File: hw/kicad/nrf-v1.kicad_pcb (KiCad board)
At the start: 2 copper layers, 25 parts, among them U1 TPS62732, U2 nRF51822, U3 SST25WF040B, U4 BMA280, U5 SI7053

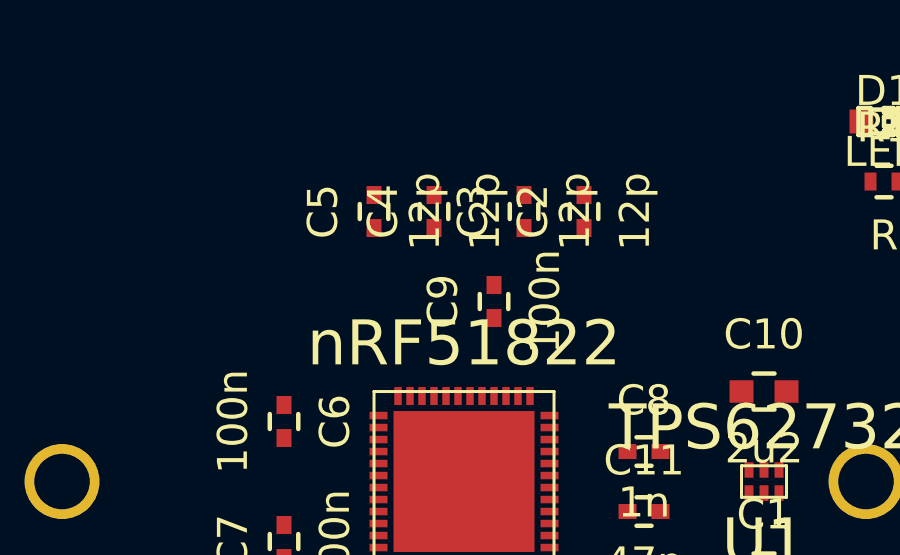
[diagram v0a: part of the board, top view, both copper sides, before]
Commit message: Add crystals
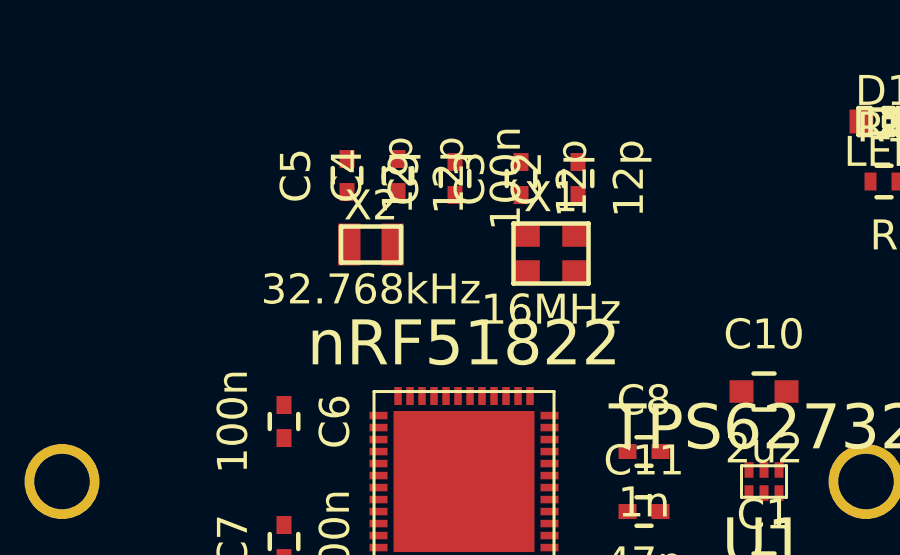
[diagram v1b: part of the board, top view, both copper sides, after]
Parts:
- added X1: 16MHz, project:Abracon-ABM10, F.Cu at (102.9, 92.4)
- added X2: 32.768kHz, project:Abracon-ABS06, F.Cu at (96.9, 92.1)
- moved C9 4.30 mm to (99.7, 89.9)
- moved C4 1.70 mm to (97.8, 89.8)
- moved C5 1.50 mm to (96.1, 89.8)
- moved C2 1.12 mm to (103.8, 89.9)
- moved C3 1.10 mm to (101.9, 89.9)
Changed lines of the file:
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@@
 (kicad_pcb (version 4) (host pcbnew "(2014-10-24 BZR 5221)-product")
   (general
-    (links 59)
-    (no_connects 59)
+    (links 65)
+    (no_connects 65)
     (area 0 0 0 0)
     (thickness 1.6)
@@
     (tracks 0)
     (zones 0)
-    (modules 25)
+    (modules 27)
     (nets 65)
   )
@@
     (mod_text_size 1 1)
     (mod_text_width 0.15)
-    (pad_size 4 4)
+    (pad_size 0.9 0.8)
     (pad_drill 0)
     (pad_to_mask_clearance 0)
@@
   )
   (module Capacitors_SMD:C_0402 (layer F.Cu)
-    (at 104 91 90)
+    (at 103.8 89.9 90)
     (descr "Capacitor SMD 0402, reflow soldering, AVX (see smccp.pdf)")
     (tags "capacitor 0402")
@@
   )
   (module Capacitors_SMD:C_0402 (layer F.Cu)
-    (at 102 91 90)
+    (at 101.9 89.9 90)
     (descr "Capacitor SMD 0402, reflow soldering, AVX (see smccp.pdf)")
     (tags "capacitor 0402")
@@
   )
   (module Capacitors_SMD:C_0402 (layer F.Cu)
-    (at 99 91 90)
+    (at 97.8 89.8 90)
     (descr "Capacitor SMD 0402, reflow soldering, AVX (see smccp.pdf)")
     (tags "capacitor 0402")
@@
   )
   (module Capacitors_SMD:C_0402 (layer F.Cu)
-    (at 97 91 90)
+    (at 96.1 89.8 90)
     (descr "Capacitor SMD 0402, reflow soldering, AVX (see smccp.pdf)")
     (tags "capacitor 0402")
@@
   )
   (module Capacitors_SMD:C_0402 (layer F.Cu)
-    (at 101 94 90)
+    (at 99.7 89.9 90)
     (descr "Capacitor SMD 0402, reflow soldering, AVX (see smccp.pdf)")
     (tags "capacitor 0402")
@@
       (net 2 GND))
   )
+  (module project:Abracon-ABM10 (layer F.Cu)
+    (at 102.9 92.4 180)
+    (fp_text reference X1 (at 0 1.875 180) (layer F.SilkS)
+      (effects (font (size 1 1) (thickness 0.15)))
+    )
+    (fp_text value 16MHz (at 0 -1.875 180) (layer F.SilkS)
+      (effects (font (size 1 1) (thickness 0.15)))
+    )
+    (fp_line (start -1.25 -1) (end 1.25 -1) (layer F.SilkS) (width 0.15))
+    (fp_line (start 1.25 -1) (end 1.25 1) (layer F.SilkS) (width 0.15))
+    (fp_line (start 1.25 1) (end -1.25 1) (layer F.SilkS) (width 0.15))
+    (fp_line (start -1.25 1) (end -1.25 -1) (layer F.SilkS) (width 0.15))
+    (pad 1 smd rect (at -0.825 0.625 180) (size 0.9 0.8) (layers F.Cu F.Paste F.Mask)
+      (net 3 "Net-(C2-Pad1)"))
+    (pad 2 smd rect (at 0.825 0.625 180) (size 0.9 0.8) (layers F.Cu F.Paste F.Mask)
+      (net 2 GND))
+    (pad 3 smd rect (at 0.825 -0.625 180) (size 0.9 0.8) (layers F.Cu F.Paste F.Mask)
+      (net 4 "Net-(C3-Pad1)"))
+    (pad 4 smd rect (at -0.825 -0.625 180) (size 0.9 0.8) (layers F.Cu F.Paste F.Mask)
+      (net 2 GND))
+  )
+  (module project:Abracon-ABS06 (layer F.Cu)
+    (at 96.9 92.1 180)
+    (fp_text reference X2 (at 0 1.3 180) (layer F.SilkS)
+      (effects (font (size 1 1) (thickness 0.15)))
+    )
+    (fp_text value 32.768kHz (at 0 -1.5 180) (layer F.SilkS)
+      (effects (font (size 1 1) (thickness 0.15)))
+    )
+    (fp_line (start -1 -0.6) (end 1 -0.6) (layer F.SilkS) (width 0.15))
+    (fp_line (start 1 -0.6) (end 1 0.6) (layer F.SilkS) (width 0.15))
+    (fp_line (start 1 0.6) (end -1 0.6) (layer F.SilkS) (width 0.15))
+    (fp_line (start -1 0.6) (end -1 -0.6) (layer F.SilkS) (width 0.15))
+    (pad 1 smd rect (at -0.725 0 180) (size 0.75 1.4) (layers F.Cu F.Paste F.Mask)
+      (net 5 "Net-(C4-Pad1)"))
+    (pad 2 smd rect (at 0.725 0 180) (size 0.75 1.4) (layers F.Cu F.Paste F.Mask)
+      (net 6 "Net-(C5-Pad1)"))
+  )
 )

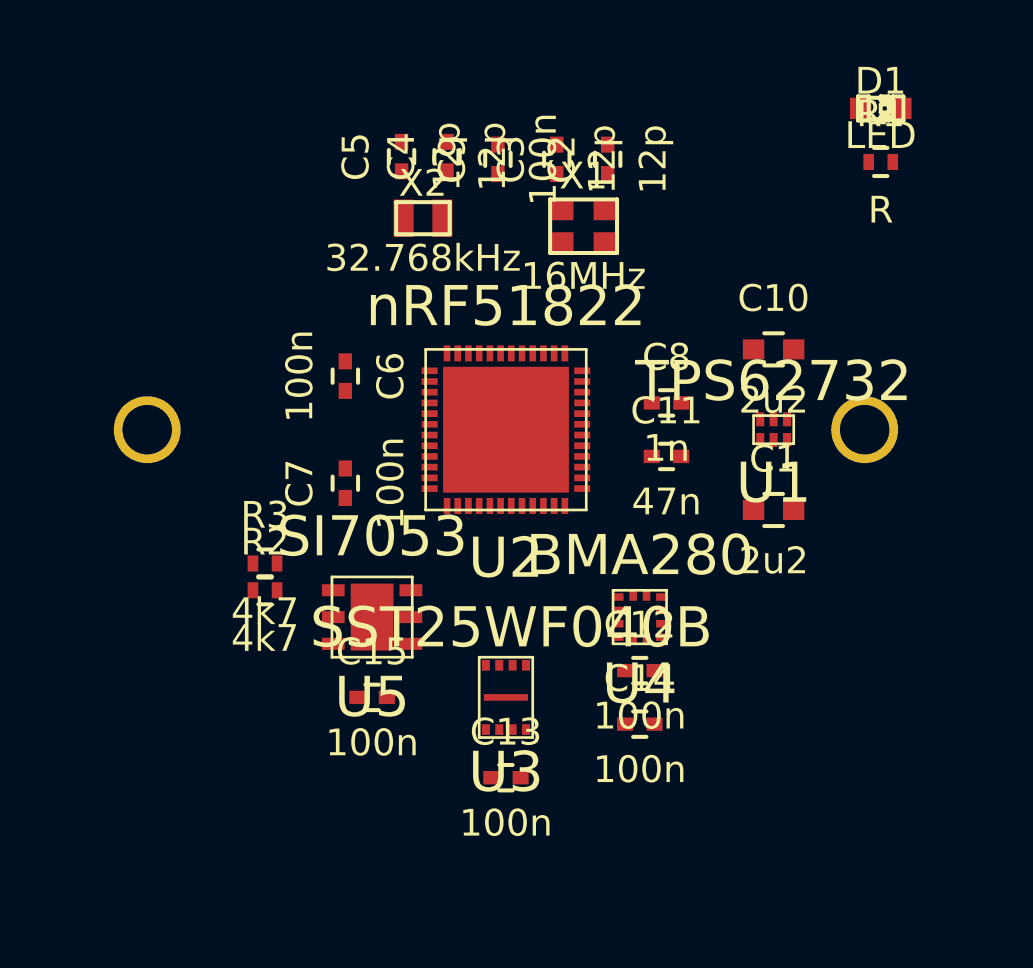
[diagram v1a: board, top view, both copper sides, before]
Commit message: Change coin cell holder
From 25mm to 20mm
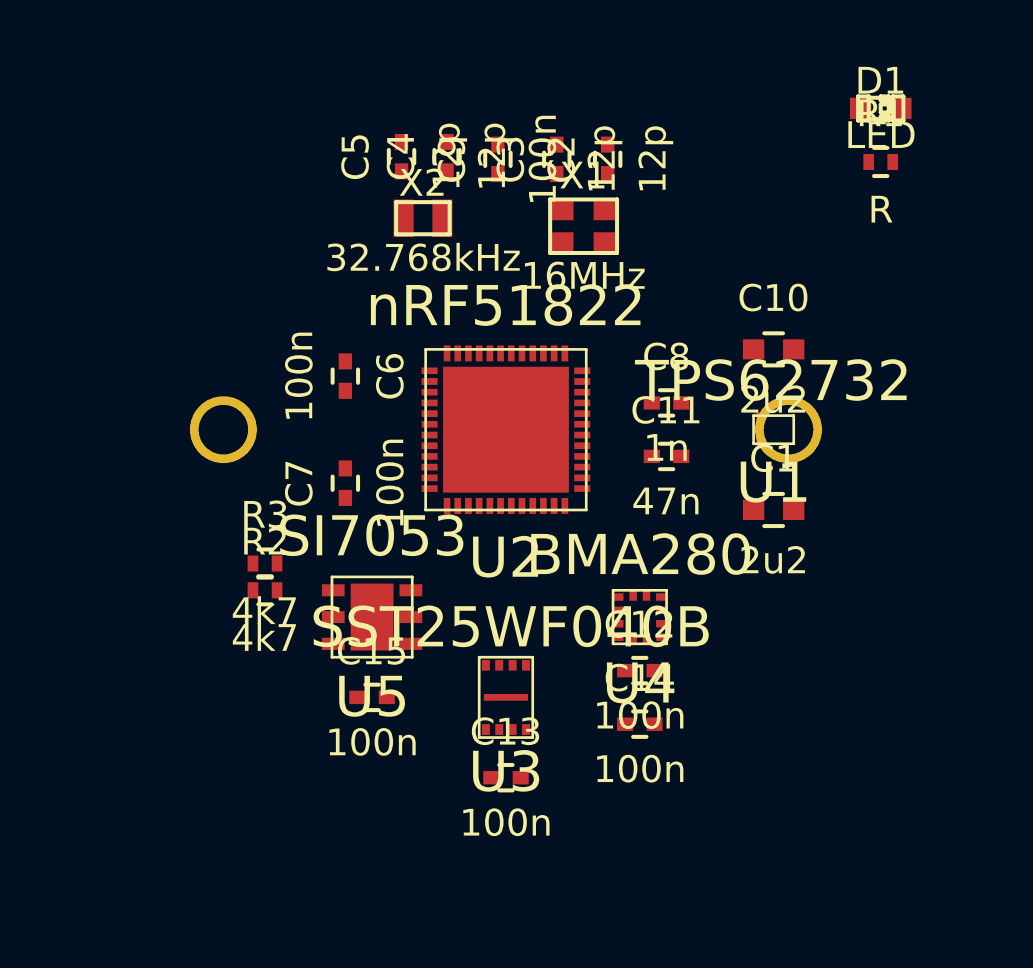
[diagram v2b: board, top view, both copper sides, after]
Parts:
- BT1: footprint project:Keystone-3007 -> project:Keystone-3003
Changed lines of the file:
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@@
   (general
     (links 65)
-    (no_connects 65)
+    (no_connects 64)
     (area 0 0 0 0)
     (thickness 1.6)
@@
     (mod_text_size 1 1)
     (mod_text_width 0.15)
-    (pad_size 0.9 0.8)
+    (pad_size 4 4)
     (pad_drill 0)
     (pad_to_mask_clearance 0)
@@
       (net 12 twi_scl))
   )
-  (module project:Keystone-3007 (layer B.Cu)
-    (at 100 100)
-    (fp_text reference BT1 (at 0.6 5.2) (layer B.SilkS)
-      (effects (font (size 1 1) (thickness 0.15)) (justify mirror))
-    )
-    (fp_text value BATTERY (at 1 6.4) (layer B.SilkS)
-      (effects (font (size 1 1) (thickness 0.15)) (justify mirror))
-    )
-    (fp_line (start 12.7 4.7) (end 11.8 4.7) (layer B.SilkS) (width 0.15))
-    (fp_line (start -12.7 4.7) (end -11.8 4.7) (layer B.SilkS) (width 0.15))
-    (fp_line (start 12.7 -4.7) (end 11.6 -4.7) (layer B.SilkS) (width 0.15))
-    (fp_line (start 11.6 -4.7) (end 3.8 -11.9) (layer B.SilkS) (width 0.15))
-    (fp_line (start -11.6 -4.7) (end -3.8 -11.9) (layer B.SilkS) (width 0.15))
-    (fp_line (start 3.8 -12.85) (end 3.8 -11.9) (layer B.SilkS) (width 0.15))
-    (fp_line (start -3.8 -12.85) (end -3.8 -11.9) (layer B.SilkS) (width 0.15))
-    (fp_line (start -12.7 -4.7) (end -11.6 -4.7) (layer B.SilkS) (width 0.15))
-    (fp_circle (center 0 0) (end 12.5 0) (layer B.SilkS) (width 0.15))
-    (fp_line (start 12.7 -4.71) (end 12.7 4.71) (layer B.SilkS) (width 0.15))
-    (fp_line (start -12.7 -4.71) (end -12.7 4.71) (layer B.SilkS) (width 0.15))
-    (fp_line (start -3.8 -12.85) (end 3.8 -12.85) (layer B.SilkS) (width 0.15))
-    (pad 1 thru_hole circle (at -13.4 0) (size 2.5 2.5) (drill 1.85) (layers *.Cu *.Mask B.SilkS)
-      (net 1 +BATT))
-    (pad 1 thru_hole circle (at 13.4 0) (size 2.5 2.5) (drill 1.85) (layers *.Cu *.Mask B.SilkS)
-      (net 1 +BATT))
-    (pad 2 smd rect (at 0 0) (size 4 4) (layers B.Cu B.Paste B.Mask)
-      (net 2 GND))
-  )
   (module project:Abracon-ABM10 (layer F.Cu)
     (at 102.9 92.4 180)
@@
       (net 6 "Net-(C5-Pad1)"))
   )
+  (module project:Keystone-3003 (layer B.Cu)
+    (at 100 100)
+    (fp_text reference BT1 (at 0.6 5.2) (layer B.SilkS)
+      (effects (font (size 1 1) (thickness 0.15)) (justify mirror))
+    )
+    (fp_text value BATTERY (at 1 6.4) (layer B.SilkS)
+      (effects (font (size 1 1) (thickness 0.15)) (justify mirror))
+    )
+    (fp_circle (center 0 0) (end 10 0) (layer B.SilkS) (width 0.15))
+    (fp_line (start -3.8 -10.58) (end 3.8 -10.58) (layer B.SilkS) (width 0.15))
+    (pad 1 thru_hole circle (at -10.555 0) (size 2.5 2.5) (drill 1.85) (layers *.Cu *.Mask B.SilkS)
+      (net 1 +BATT))
+    (pad 1 thru_hole circle (at 10.555 0) (size 2.5 2.5) (drill 1.85) (layers *.Cu *.Mask B.SilkS)
+      (net 1 +BATT))
+    (pad 2 smd rect (at 0 0) (size 4 4) (layers B.Cu B.Paste B.Mask)
+      (net 2 GND))
+  )
 )

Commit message: Component placement draft
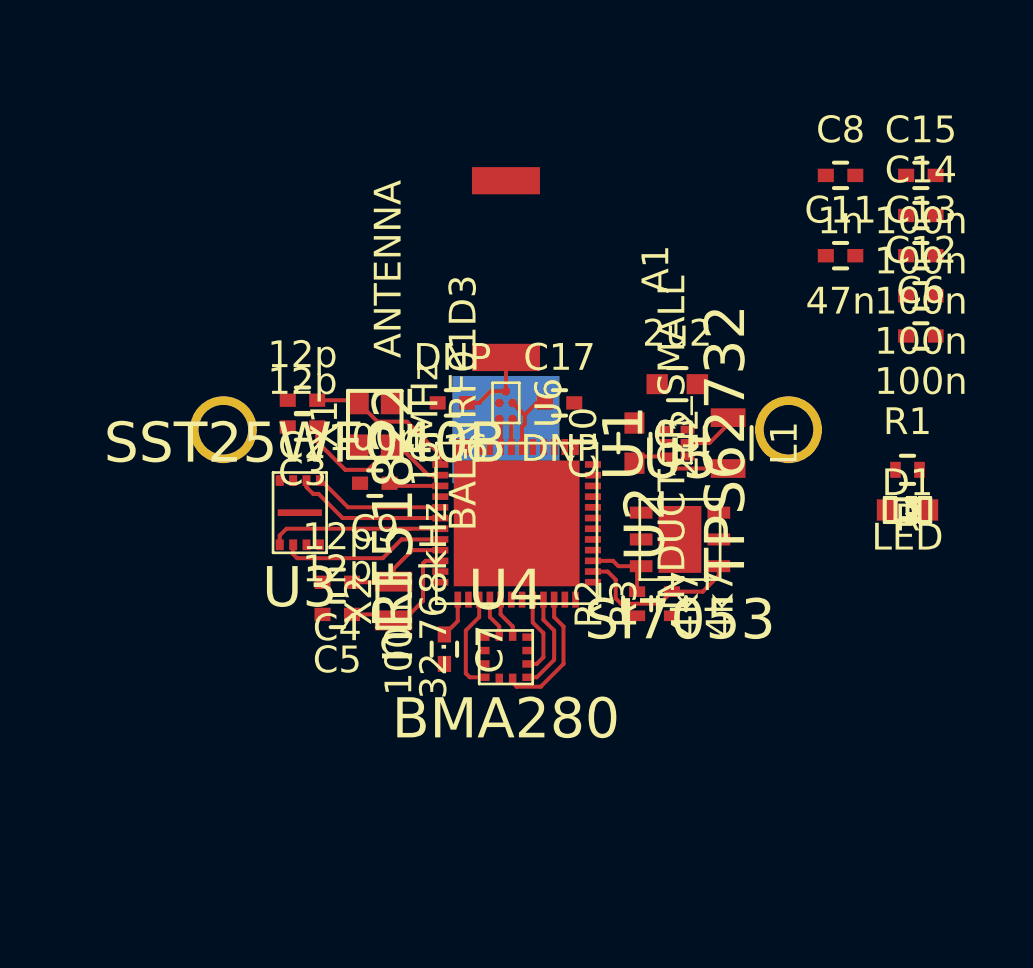
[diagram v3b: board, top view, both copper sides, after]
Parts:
- added A1: ANTENNA, project:AntennaFactor-ANT-2.4-CHP, F.Cu at (100.0, 94.0)
- added C16: DNP, Capacitors_SMD:C_0402, F.Cu at (98.0, 99.0)
- added C17: DNP, Capacitors_SMD:C_0402, F.Cu at (102.0, 99.0)
- added L1: INDUCTOR_SMALL, Resistors_SMD:R_0805, F.Cu at (108.3, 100.5)
- added U6: BAL-NRF01D3, project:ST-BGA-5_(1.50x1.00), F.Cu at (100.0, 99.0)
- moved C15 28.3 mm to (115.5, 90.5)
- moved C13 24.9 mm to (115.5, 93.5)
- moved C14 21.7 mm to (115.5, 92.0)
- moved C6 21.6 mm to (115.5, 96.5), turned to 0 degrees
- moved C12 17.5 mm to (115.5, 95.0)
- moved C5 17.3 mm to (93.7, 106.9), turned to 180 degrees
- moved C4 16.4 mm to (93.7, 105.7), turned to 180 degrees
- moved R3 15.3 mm to (106.2, 106.5), turned to 90 degrees
- moved D1 15.0 mm to (115.0, 103.0)
- moved C2 14.5 mm to (92.4, 98.9), turned to 180 degrees
- moved X2 14.3 mm to (95.8, 106.4), turned to 270 degrees
- moved R2 13.9 mm to (104.9, 106.5), turned to 90 degrees
- moved C3 13.8 mm to (92.4, 99.9), turned to 180 degrees
- moved C9 12.9 mm to (95.1, 102.0), turned to 180 degrees
- moved U5 11.9 mm to (106.5, 104.1), turned to 180 degrees
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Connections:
- C10 pad 1: Net-(C10-Pad1) -> VDD
- U2 pad 10: Net-(U2-Pad10) -> spi1_sck
- U2 pad 14: Net-(U2-Pad14) -> twi_sda
- U2 pad 15: Net-(U2-Pad15) -> twi_scl
- U2 pad 3: Net-(U2-Pad3) -> spi1_cs_n
- U2 pad 4: Net-(U2-Pad4) -> acc_int2
- U2 pad 41: Net-(U2-Pad41) -> spi0_cs_n
- U2 pad 42: Net-(U2-Pad42) -> spi0_miso
- U2 pad 43: Net-(U2-Pad43) -> spi0_mosi
- U2 pad 44: Net-(U2-Pad44) -> spi0_sck
- U2 pad 5: Net-(U2-Pad5) -> acc_int1
- U2 pad 8: Net-(U2-Pad8) -> spi1_mosi
- U2 pad 9: Net-(U2-Pad9) -> spi1_miso
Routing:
- net spi0_mosi: track 0.00 -> 6.45 mm
- net Net-(C3-Pad1): track 0.00 -> 6.39 mm
- net twi_sda: track 0.00 -> 6.39 mm
- net spi0_sck: track 0.00 -> 6.20 mm
- net Net-(C2-Pad1): track 0.00 -> 5.80 mm
- net spi0_miso: track 0.00 -> 5.73 mm
- net VDD: track 0.00 -> 5.30 mm
- net Net-(C5-Pad1): track 0.00 -> 5.13 mm
- net spi1_sck: track 0.00 -> 4.99 mm
- net spi0_cs_n: track 0.00 -> 4.91 mm
- net Net-(C4-Pad1): track 0.00 -> 4.08 mm
- net spi1_cs_n: track 0.00 -> 3.70 mm
- net spi1_miso: track 0.00 -> 3.67 mm
- net spi1_mosi: track 0.00 -> 3.00 mm
- net twi_scl: track 0.00 -> 2.89 mm
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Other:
- net class Default: clearance 0.254 -> 0.1; trace_width 0.254 -> 0.2; via_dia 0.889 -> 0.3; via_drill 0.635 -> 0.15
- rule trace_clearance: 0.254 -> 0.1
- rule trace_min: 0.254 -> 0.15
- rule via_min_drill: 0.508 -> 0.15
- rule via_min_size: 0.889 -> 0.3

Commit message: Updated coin cell holder
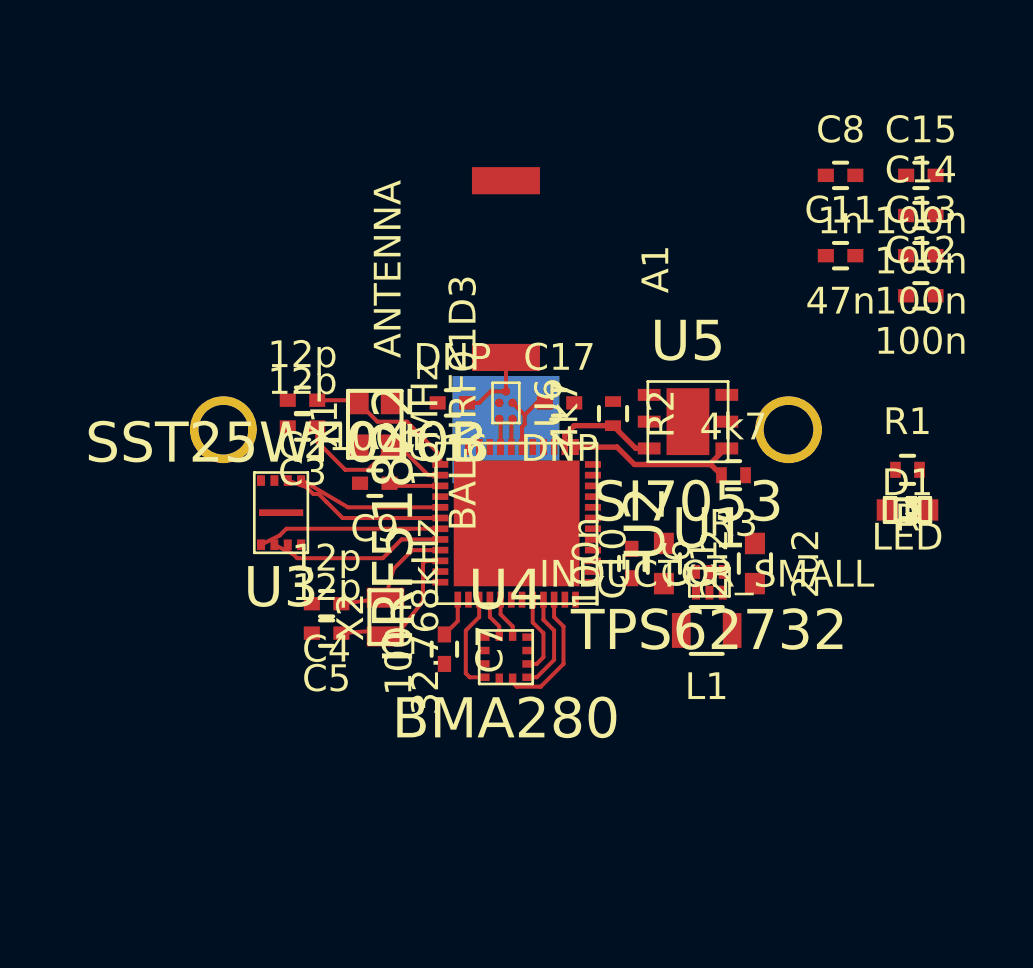
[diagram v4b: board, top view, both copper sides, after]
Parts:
- moved C6 13.7 mm to (104.7, 105.0), turned to 270 degrees
- moved C1 7.30 mm to (109.3, 105.0), turned to 90 degrees
- moved R2 7.16 mm to (104.0, 99.4), turned to 270 degrees
- moved L1 7.05 mm to (107.5, 107.5), turned to 180 degrees
- moved U1 5.34 mm to (107.6, 105.7), turned to 180 degrees
- moved R3 5.32 mm to (108.5, 101.7), turned to 180 degrees
- moved C10 4.63 mm to (105.9, 105.0)
- moved U5 4.41 mm to (106.8, 99.7)
- moved C4 0.89 mm to (93.3, 106.5)
- moved C5 0.81 mm to (93.3, 107.6)
- moved U3 0.70 mm to (91.6, 103.1)
- moved X2 0.67 mm to (95.5, 107.0)
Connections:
- U2 pad 14: twi_sda -> Net-(U2-Pad14)
- U2 pad 15: twi_scl -> Net-(U2-Pad15)
- U2 pad 25: Net-(U2-Pad25) -> twi_sda
- U2 pad 26: Net-(U2-Pad26) -> twi_scl
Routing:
- net VDD: track 5.30 -> 1.51 mm
- net Net-(L1-Pad1): track 2.15 -> 0.00 mm
- net twi_scl: track 2.89 -> 4.10 mm
- net Net-(C5-Pad1): track 5.13 -> 5.89 mm
- net Net-(C4-Pad1): track 4.08 -> 4.83 mm
- net spi0_cs_n: track 4.91 -> 5.47 mm
